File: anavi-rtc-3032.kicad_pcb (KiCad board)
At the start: 2 copper layers, 9 parts, among them J1 Conn_01x06_Pin, U1 RV-3032

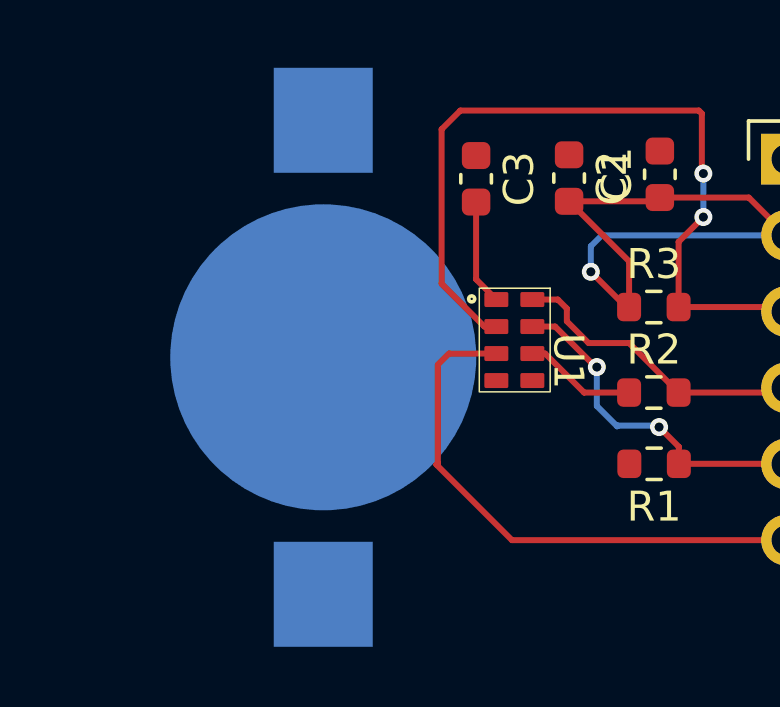
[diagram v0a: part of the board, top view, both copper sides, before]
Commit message: Fix ERC issues in schematics
Fix issues in the Electrical Rules Checker (ERC) for the schematics.

Signed-off-by: Leon Anavi <leon@anavi.org>
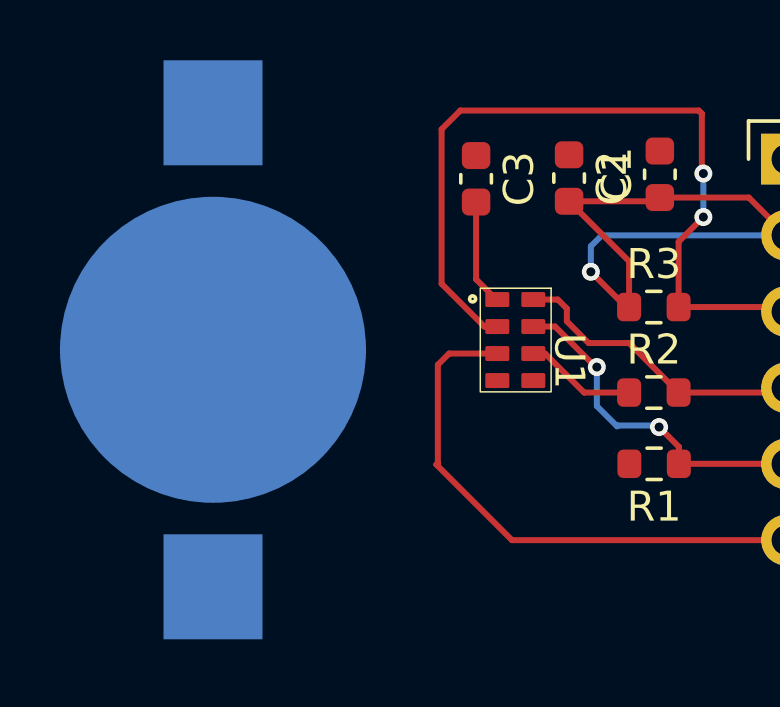
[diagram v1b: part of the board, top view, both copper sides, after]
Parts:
- removed BT2: KEYSTONE 3000, Battery:BatteryHolder_Keystone_3000_1x12mm
- added BT1: Battery_Cell, Battery:BatteryHolder_Keystone_3000_1x12mm, B.Cu at (77.6, 44.1)
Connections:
- C3 pad 1: Net-(BT2--) -> GND

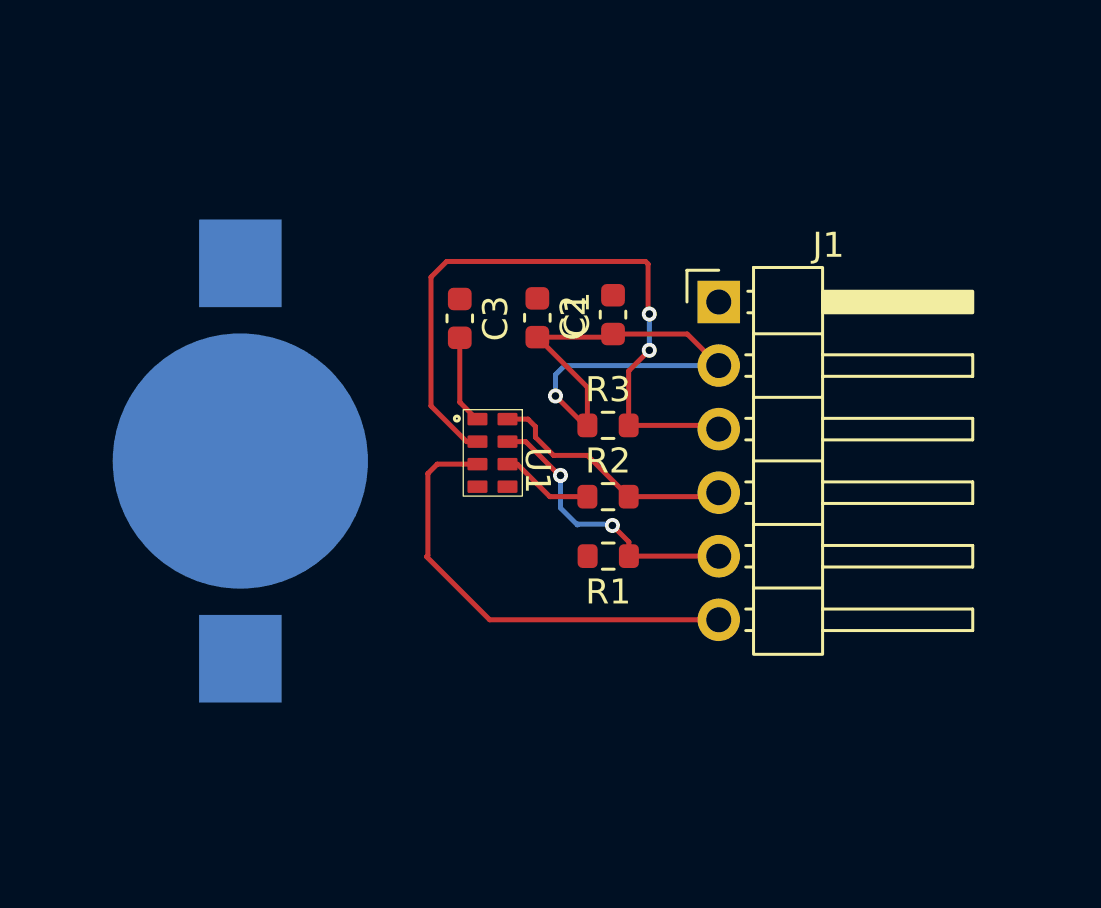
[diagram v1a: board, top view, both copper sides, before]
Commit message: Printed Circuit Board
Add the PCB design for hardware revision 1.0.

Signed-off-by: Leon Anavi <leon@anavi.org>
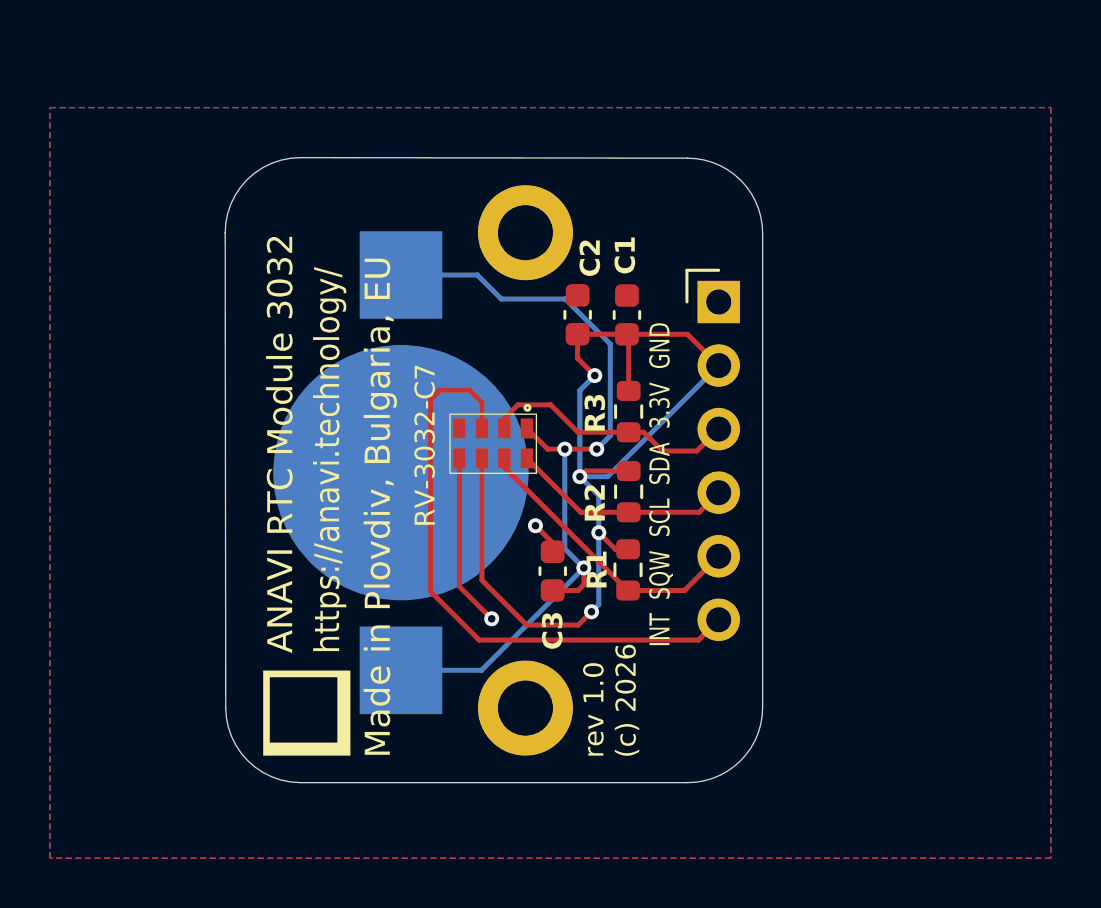
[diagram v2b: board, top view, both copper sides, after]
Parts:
- removed BT1: Battery_Cell, Battery:BatteryHolder_Keystone_3000_1x12mm
- added CR1216 Battery: Battery_Cell, Battery:BatteryHolder_Keystone_3000_1x12mm, B.Cu at (84.0, 44.6)
- added G***: LOGO, logo:anavi-logo, F.Cu at (80.3, 54.2)
- added REF**: MountingHole_2.2mm_M2_DIN965_Pad, MountingHole:MountingHole_2.2mm_M2_DIN965_Pad, F.Cu at (89.0, 35.0)
- added REF**: MountingHole_2.2mm_M2_DIN965_Pad, MountingHole:MountingHole_2.2mm_M2_DIN965_Pad, F.Cu at (89.0, 54.0)
- J1: footprint Connector_PinHeader_2.54mm:PinHeader_1x06_P2.54mm_Horizontal -> lib:PinHeader_1x06_P2.54mm_Horizontal-mod
- moved C3 10.8 mm to (90.1, 48.5)
- moved C2 1.61 mm to (91.1, 38.3)
- moved R3 0.99 mm to (93.1, 42.1), turned to -90 degrees
- moved R1 0.96 mm to (93.1, 48.5), turned to 90 degrees
- moved R2 0.85 mm to (93.1, 45.4), turned to -90 degrees
- moved C1 0.56 mm to (93.1, 38.3)
- moved RV-3032-C7 0.38 mm to (87.7, 43.4), turned to 180 degrees
- renumbered U1 to RV-3032-C7
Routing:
- net Net-(BT1-+): track 3.53 -> 33.2 mm, vias 0 -> 3
- net I2C_SDA_OTHER: track 27.0 -> 10.4 mm, vias 2 -> 0
- net +3V3: track 25.2 -> 41.6 mm, vias 1 -> 4
- net GND: track 0.00 -> 8.27 mm, vias 0 -> 2
- net RTC_INT: track 18.2 -> 23.8 mm
- net I2C_SCL_OTHER: track 10.1 -> 8.88 mm
- net RTC_SQW: vias 2 -> 0
- added copper zone on B.Cu, net GND
- added copper zone on F.Cu, net GND
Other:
- board outline added: 21.5 x 25 mm
- board text added: "ANAVI RTC Module 3032"
- board text added: "GND 3.3V SDA SCL SQW INT"
- board text added: "INT SQW SCL SDA 3.3V GND"
- board text added: "Made in Plovdiv, Bulgaria, EU"
- board text added: "https://anavi.technology/"
- board text added: "rev 1.0 (c) 2026"

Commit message: Add fabrication details
Adjust the PCB layers to add fabrication details.

Signed-off-by: Leon Anavi <leon@anavi.org>
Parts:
- R2, R3: value 2.2 kΩ -> 4.7k
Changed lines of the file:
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@@
 			(at 0 2.85 0)
 			(layer "F.Fab")
+			(hide yes)
 			(effects
 				(font
@@
 			)
 		)
-		(property "Value" "2.2 kΩ"
-			(at 0 1.43 90)
+		(property "Value" "4.7k"
+			(at 0.05 -1.375 90)
 			(layer "F.Fab")
 			(effects
@@
 			(at 0 2.85 0)
 			(layer "F.Fab")
+			(hide yes)
 			(effects
 				(font
@@
 			(at 4.385 14.97 0)
 			(layer "F.Fab")
+			(hide yes)
 			(effects
 				(font
@@
 			)
 		)
-		(property "Value" "2.2 kΩ"
-			(at 0 1.43 90)
+		(property "Value" "4.7k"
+			(at -0.025814 -1.375 90)
 			(layer "F.Fab")
 			(effects
@@
 			(unlocked yes)
 			(layer "F.Fab")
-			(effects
-				(font
+			(hide yes)
+			(effects
+				(font

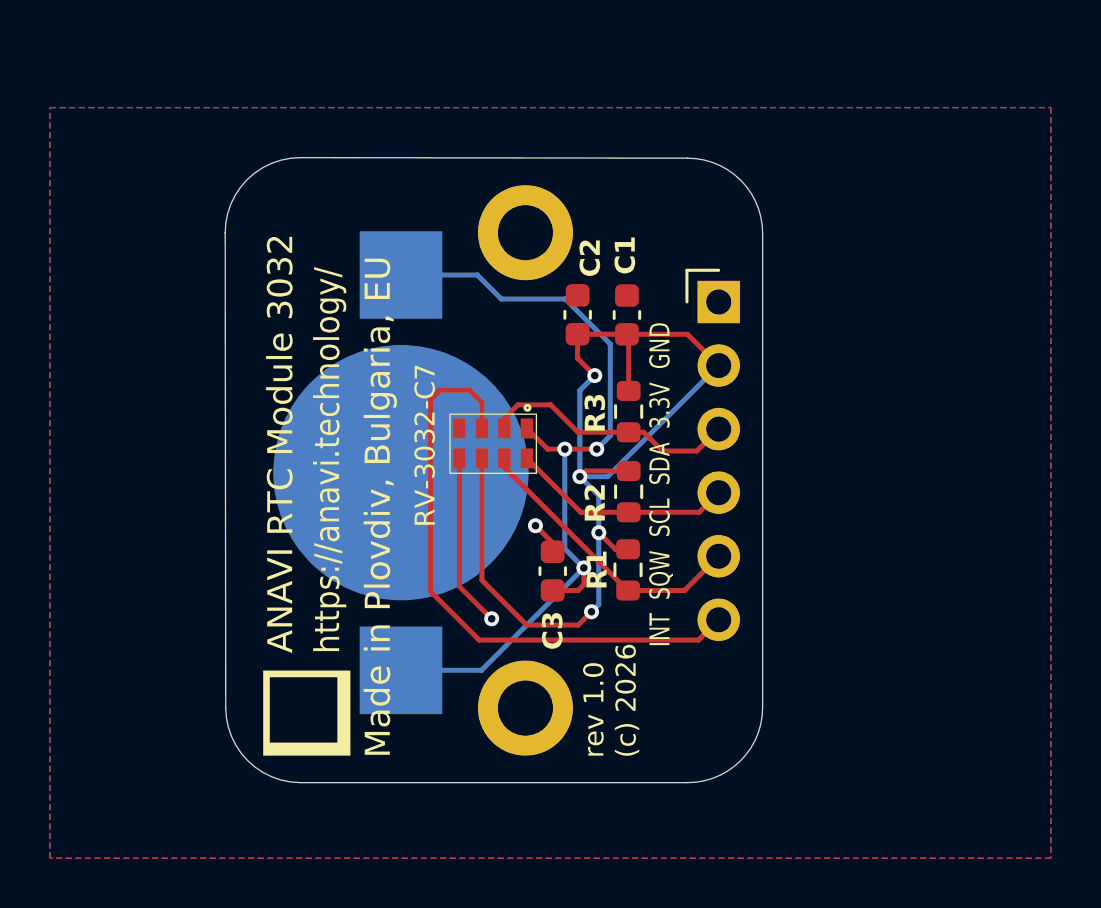
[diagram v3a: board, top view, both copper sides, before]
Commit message: Change PCB output
Change the shape of the PCB outline and adjust labels.

Signed-off-by: Leon Anavi <leon@anavi.org>
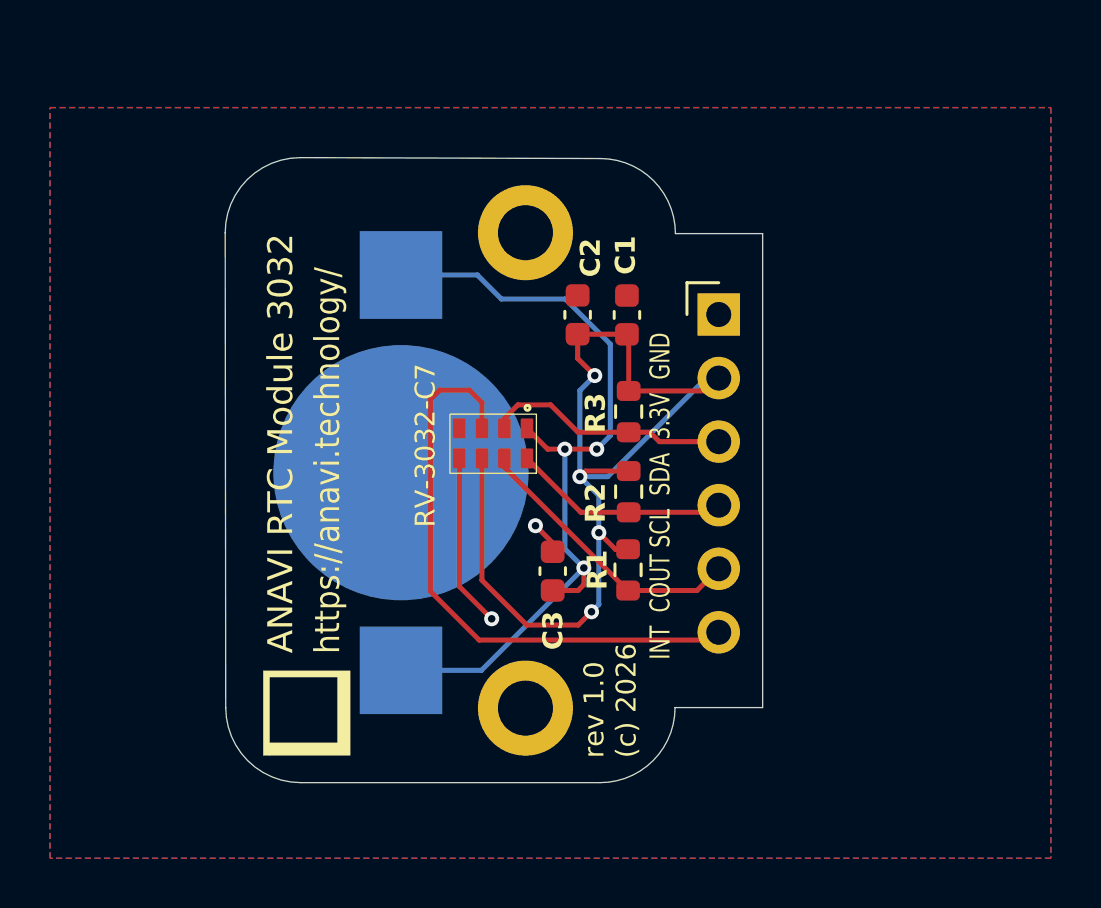
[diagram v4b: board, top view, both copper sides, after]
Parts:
- moved J1 0.50 mm to (96.7, 38.3)
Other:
- outline, holes or cut-outs redrawn
- board text added: "GND 3.3V SDA SCL COUT INT"
- board text added: "INT COUT SCL SDA 3.3V GND"
- board text removed: "GND 3.3V SDA SCL SQW INT"
- board text removed: "INT SQW SCL SDA 3.3V GND"
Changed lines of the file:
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@@
 			(drillshape 0)
 			(scaleselection 1)
-			(outputdirectory "plots/anavi-rtc-3032-r10/")
+			(outputdirectory "plots/anavi-rtc-3032-r10a/")
 		)
 	)
@@
 	(footprint "lib:PinHeader_1x06_P2.54mm_Horizontal-mod"
 		(layer "F.Cu")
-		(at 96.725 37.77)
+		(at 96.725 38.27)
 		(descr "Through hole angled pin header, 1x06, 2.54mm pitch, 6mm pin length, single row")
 		(tags "Through hole angled pin header THT 1x06 2.54mm single row")
@@
 	(gr_line
 		(start 80 32)
-		(end 95.47868 32.02132)
+		(end 91.993343 32.035983)
 		(stroke
 			(width 0.05)
@@
 		(layer "Edge.Cuts")
 	)
+	(gr_line
+		(start 91.97868 56.97868)
+		(end 80.02132 56.97868)
+		(stroke
+			(width 0.05)
+			(type default)
+		)
+		(layer "Edge.Cuts")
+	)
 	(gr_arc
-		(start 95.47868 32.02132)
-		(mid 97.600006 32.899994)
-		(end 98.47868 35.02132)
+		(start 91.993343 32.035983)
+		(mid 94.114669 32.914657)
+		(end 94.993343 35.035983)
 		(stroke
 			(width 0.05)
@@
 		(layer "Edge.Cuts")
 	)
-	(gr_line
-		(start 95.47868 56.97868)
-		(end 80.02132 56.97868)
+	(gr_arc
+		(start 94.97868 53.97868)
+		(mid 94.100006 56.100006)
+		(end 91.97868 56.97868)
 		(stroke
 			(width 0.05)
@@
 	)
 	(gr_line
-		(start 98.47868 35.02132)
+		(start 94.97868 53.97868)
 		(end 98.47868 53.97868)
 		(stroke
@@
 		(layer "Edge.Cuts")
 	)
-	(gr_arc
-		(start 98.47868 53.97868)
-		(mid 97.600006 56.100006)
-		(end 95.47868 56.97868)
+	(gr_line
+		(start 94.993343 35.035983)
+		(end 98.47868 35.035983)
 		(stroke
 			(width 0.05)
@@
 		(layer "Edge.Cuts")
 	)
-	(gr_text "INT  SQW  SCL  SDA  3.3V  GND"
-		(at 94.853368 51.564037 90)
+	(gr_line
+		(start 98.47868 35.035983)
+		(end 98.47868 53.97868)
+		(stroke
+			(width 0.05)
+			(type default)
+		)
+		(layer "Edge.Cuts")
+	)
+	(gr_text "INT  COUT SCL  SDA  3.3V  GND"
+		(at 94.853368 52.064037 90)
 		(layer "F.SilkS")
 		(effects
@@
 		)
 	)
-	(gr_text "Made in Plovdiv, Bulgaria, EU"
-		(at 83.7 56 90)
+	(gr_text "ANAVI RTC Module 3032\n"
+		(at 79.8 51.808577 90)
 		(layer "F.SilkS")
 		(effects
 			(font
 				(size 1 1)
-				(thickness 0.1)
+				(thickness 0.15)
 			)
 			(justify left bottom)
 		)
 	)
-	(gr_text "ANAVI RTC Module 3032\n"
-		(at 79.8 51.808577 90)
-		(layer "F.SilkS")
+	(gr_text "Made in Plovdiv,\nBulgaria, EU"
+		(at 86.8 34.6 0)
+		(layer "B.SilkS")
 		(effects
 			(font
-				(size 1 1)
-				(thickness 0.15)
+				(size 0.8 0.6)
+				(thickness 0.1)
 			)
-			(justify left bottom)
+			(justify left bottom mirror)
 		)
 	)
-	(gr_text "GND  3.3V  SDA  SCL  SQW  INT"
-		(at 94.9 36.6 90)
+	(gr_text "GND  3.3V  SDA  SCL COUT  INT"
+		(at 94.9 37.1 90)
 		(layer "B.SilkS")
 		(effects
@@
 	)
 	(segment
-		(start 93.055942 39.062329)
-		(end 95.477329 39.062329)
-		(width 0.2)
-		(layer "F.Cu")
-		(net "+3V3")
-	)
-	(segment
-		(start 95.477329 39.062329)
-		(end 96.725 40.31)
+		(start 93.049213 39.0556)
+		(end 93.055942 39.062329)
 		(width 0.2)
 		(layer "F.Cu")
@@
 	)
 	(segment
-		(start 93.049213 39.0556)
-		(end 93.055942 39.062329)
+		(start 92.592893 47.65)
+		(end 91.932893 46.99)
 		(width 0.2)
 		(layer "F.Cu")
@@
 	)
 	(segment
-		(start 92.592893 47.65)
-		(end 91.932893 46.99)
+		(start 93.125 41.325)
+		(end 96.21 41.325)
 		(width 0.2)
 		(layer "F.Cu")
@@
 	)
 	(segment
+		(start 96.21 41.325)
+		(end 96.725 40.81)
+		(width 0.2)
+		(layer "F.Cu")
+		(net "+3V3")
+	)
+	(segment
 		(start 91.11 50.68)
 		(end 91.64 50.15)
@@
 	)
 	(segment
-		(start 95.94 46.175)
-		(end 96.725 45.39)
+		(start 96.44 46.175)
+		(end 96.725 45.89)
 		(width 0.2)
 		(layer "F.Cu")
@@
 	(segment
 		(start 93.125 46.175)
-		(end 95.94 46.175)
+		(end 96.44 46.175)
 		(width 0.2)
 		(layer "F.Cu")
@@
 	(segment
 		(start 93.1 49.3)
-		(end 95.355 49.3)
+		(end 95.855 49.3)
 		(width 0.2)
 		(layer "F.Cu")
@@
 	)
 	(segment
-		(start 95.355 49.3)
-		(end 96.725 47.93)
+		(start 93.084315 49.3)
+		(end 93.1 49.3)
 		(width 0.2)
 		(layer "F.Cu")
@@
 	)
 	(segment
-		(start 93.084315 49.3)
-		(end 93.1 49.3)
+		(start 95.855 49.3)
+		(end 96.725 48.43)
 		(width 0.2)
 		(layer "F.Cu")
@@
 	)
 	(segment
-		(start 94.475 43.725)
-		(end 93.725 42.975)
+		(start 96.35 43.725)
+		(end 96.725 43.35)
 		(width 0.2)
 		(layer "F.Cu")
@@
 	)
 	(segment
-		(start 88.16 42.42)
-		(end 88.7 41.88)
+		(start 93.125 42.975)
+		(end 93.975 42.975)
 		(width 0.2)
 		(layer "F.Cu")
@@
 	)
 	(segment
-		(start 93.725 42.975)
-		(end 93.125 42.975)
+		(start 88.16 42.42)
+		(end 88.7 41.88)
 		(width 0.2)
 		(layer "F.Cu")
@@
 	)
 	(segment
-		(start 95.85 43.725)
-		(end 94.475 43.725)
+		(start 93.975 42.975)
+		(end 94.35 43.35)
 		(width 0.2)
 		(layer "F.Cu")
@@
 	)
 	(segment
-		(start 96.725 42.85)
-		(end 95.85 43.725)
+		(start 88.7 41.88)
+		(end 90.006471 41.88)
 		(width 0.2)
 		(layer "F.Cu")
@@
 	)
 	(segment
-		(start 88.7 41.88)
-		(end 90.006471 41.88)
+		(start 94.35 43.35)
+		(end 96.725 43.35)
 		(width 0.2)
 		(layer "F.Cu")
@@
 	)
 	(segment
-		(start 87.26 41.79)
-		(end 86.76 41.29)
+		(start 85.57 41.29)
+		(end 85.21 41.65)
 		(width 0.2)
 		(layer "F.Cu")
@@
 	)
 	(segment
-		(start 85.57 41.29)
-		(end 85.21 41.65)
+		(start 85.21 49.34)
+		(end 87.15 51.28)
 		(width 0.2)
 		(layer "F.Cu")
@@
 	)
 	(segment
-		(start 95.915 51.28)
-		(end 96.725 50.47)
+		(start 87.26 42.82)
+		(end 87.26 41.79)
 		(width 0.2)
 		(layer "F.Cu")
@@
 	)
 	(segment
-		(start 86.76 41.29)
-		(end 85.57 41.29)
+		(start 96.415 51.28)
+		(end 96.725 50.97)
 		(width 0.2)
 		(layer "F.Cu")
@@
 	)
 	(segment
-		(start 85.21 49.34)
-		(end 87.15 51.28)
+		(start 87.15 51.28)
+		(end 96.415 51.28)
 		(width 0.2)
 		(layer "F.Cu")
@@
 	)
 	(segment
-		(start 87.26 42.82)
-		(end 87.26 41.79)
+		(start 87.26 41.79)
+		(end 86.76 41.29)
 		(width 0.2)
 		(layer "F.Cu")
@@
 	)
 	(segment
-		(start 87.15 51.28)
-		(end 95.915 51.28)
+		(start 86.76 41.29)
+		(end 85.57 41.29)
 		(width 0.2)
 		(layer "F.Cu")
